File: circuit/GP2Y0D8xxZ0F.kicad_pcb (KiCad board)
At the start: 2 copper layers, 26.7 x 24.1 mm, 13 parts, among them P1 CONN_01X04, U1 GP2Y0D81xZ0F

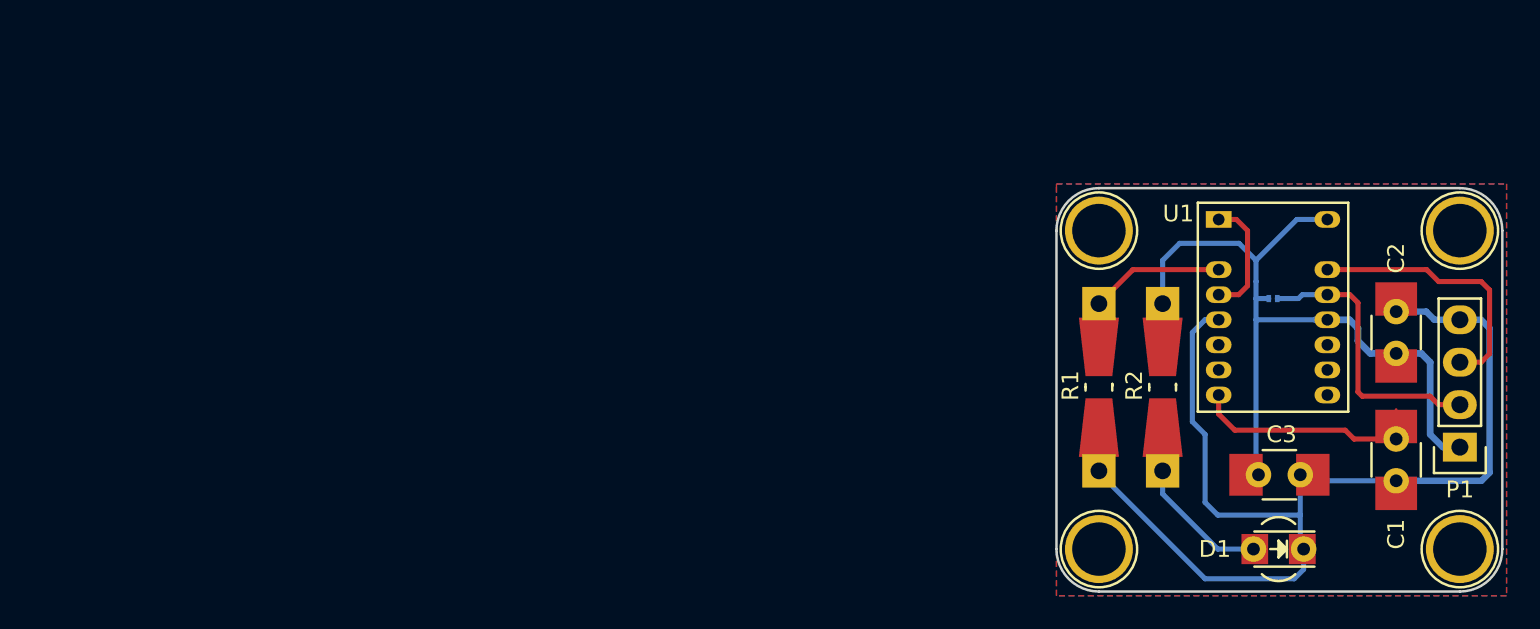
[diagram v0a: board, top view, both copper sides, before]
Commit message: First convert try and resize
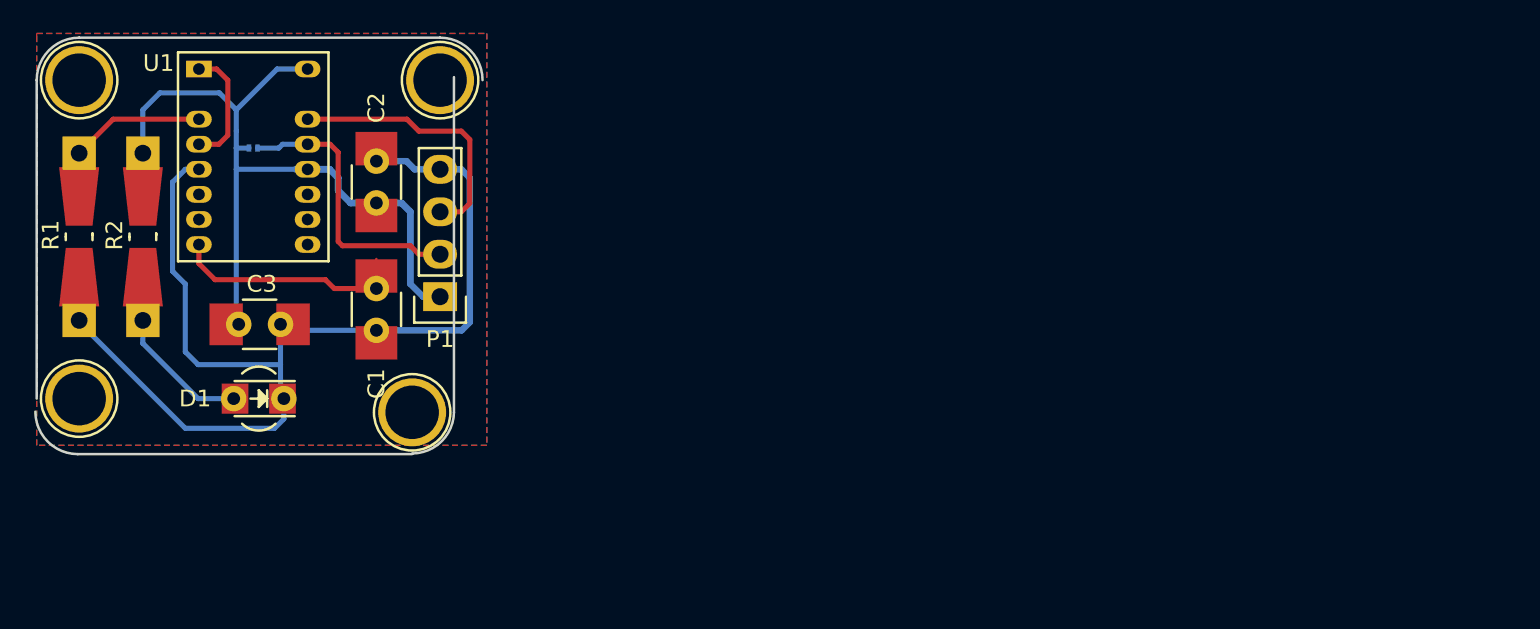
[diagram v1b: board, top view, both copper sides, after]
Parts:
- moved REF** 63.2 mm to (91.0, 98.5)
- moved C1 61.7 mm to (88.9, 92.3)
- moved C2 61.7 mm to (88.9, 84.7)
- moved R1 61.7 mm to (71.1, 88.0)
- moved REF** 61.7 mm to (71.1, 78.6)
- moved REF** 61.7 mm to (71.1, 97.7)
- moved C3 61.7 mm to (81.9, 93.2)
- moved JP1 61.7 mm to (81.5, 82.7)
- moved U1 61.7 mm to (81.5, 84.0)
- moved D1 61.7 mm to (81.8, 97.7)
- moved P1 61.7 mm to (92.7, 91.6)
- moved R2 61.7 mm to (74.9, 88.0)
- moved REF** 61.7 mm to (92.7, 78.6)
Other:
- board size 26.7 x 24.1 mm -> 26.8 x 24.9 mm

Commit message: changes in progress, open project with version 5 of kicad and the resizing started
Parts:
- moved REF** 1.68 mm to (91.0, 78.5)
- moved R2 1.02 mm to (74.0, 88.5)
- moved C3 0.91 mm to (81.0, 93.0)
- moved REF** 0.82 mm to (71.0, 98.5)
- moved R1 0.77 mm to (70.5, 88.5)
- moved U1 0.50 mm to (81.0, 84.0)
- moved REF** 0.15 mm to (71.0, 78.5)
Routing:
- net GND: track 70.0 -> 31.1 mm
- net VCC: track 50.8 -> 30.5 mm
- net Net-(D1-Pad2): track 10.8 -> 4.72 mm
- net /Output: track 16.0 -> 10.1 mm
- net /Enable: track 17.6 -> 13.2 mm
- net Net-(C1-Pad1): track 15.0 -> 13.9 mm
- removed copper zone on B.Cu, net GND
- removed copper zone on F.Cu, net GND
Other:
- board size 26.8 x 24.9 mm -> 25.1 x 25 mm

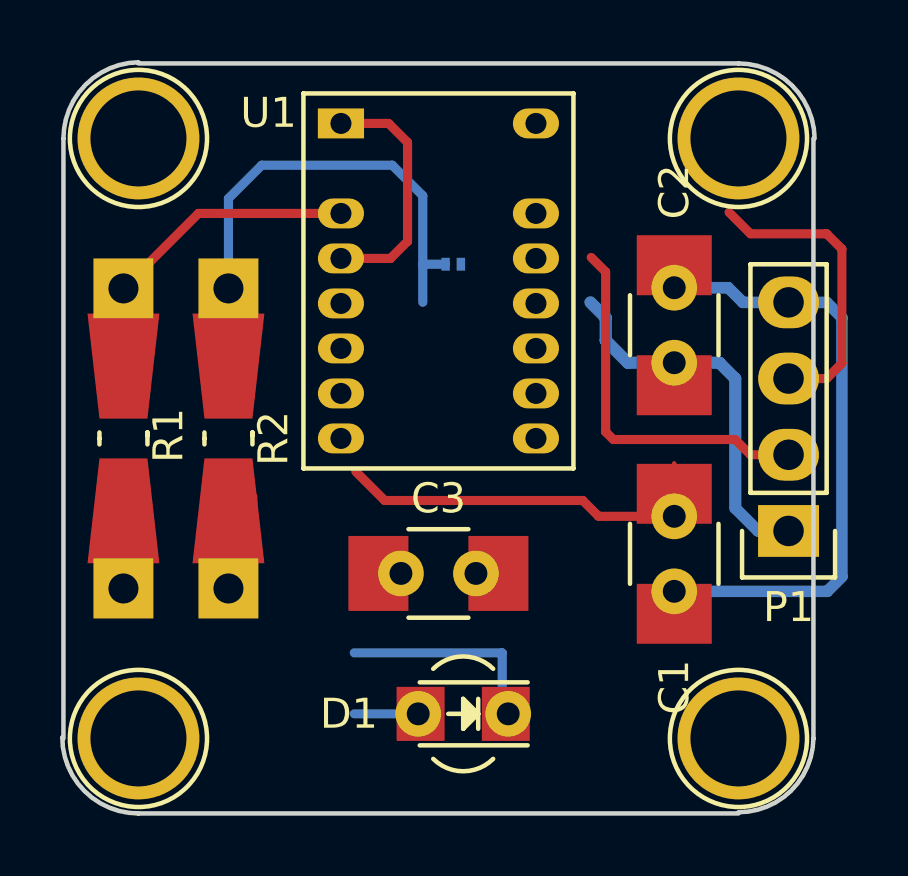
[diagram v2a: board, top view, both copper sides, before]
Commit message: New distribution of component in new size 25x25 mm
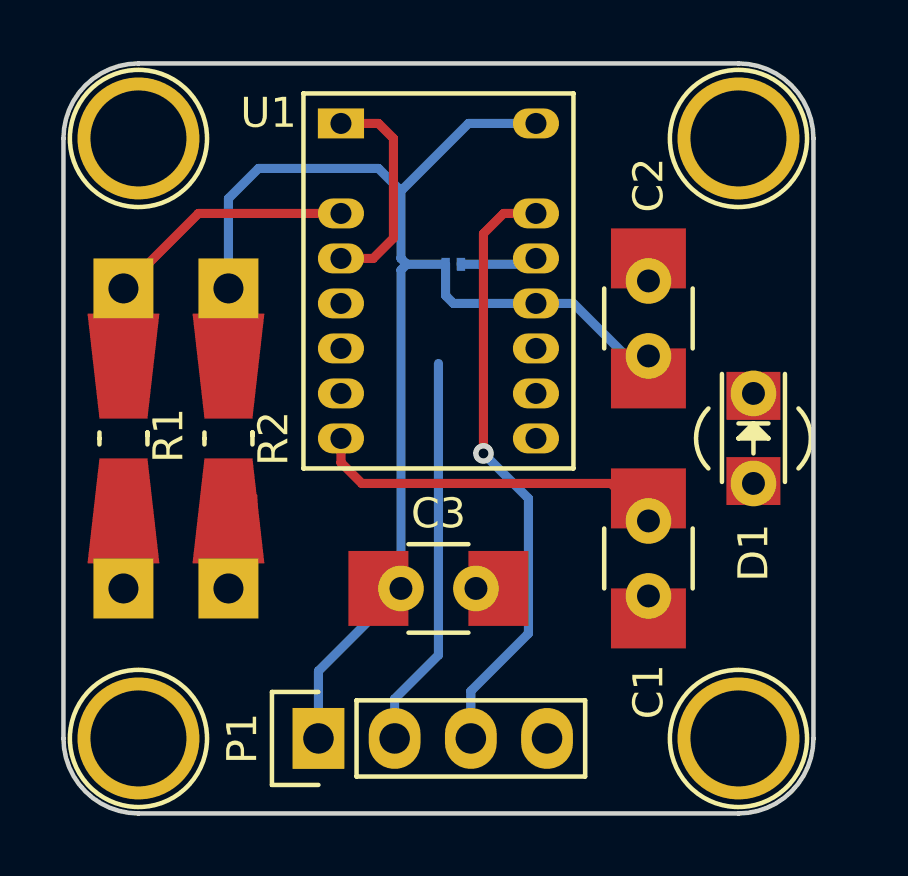
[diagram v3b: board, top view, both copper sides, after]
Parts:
- moved P1 17.1 mm to (77.0, 98.5), turned to 90 degrees
- moved D1 13.3 mm to (91.5, 88.5), turned to 270 degrees
- moved C2 0.89 mm to (88.0, 84.5)
- moved C1 0.87 mm to (88.0, 92.5)
- moved C3 0.50 mm to (81.0, 93.5)
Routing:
- net GND: track 31.1 -> 2.80 mm
- net VCC: track 30.5 -> 47.5 mm
- net /Output: track 10.1 -> 20.3 mm, vias 0 -> 1
- net /Enable: track 13.2 -> 15.7 mm
- net Net-(D1-Pad2): track 4.72 -> 2.59 mm
- net Net-(C1-Pad1): track 13.9 -> 11.9 mm
- net Net-(U1-Pad1): track 8.24 -> 7.31 mm
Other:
- board size 25.1 x 25 mm -> 25 x 25 mm

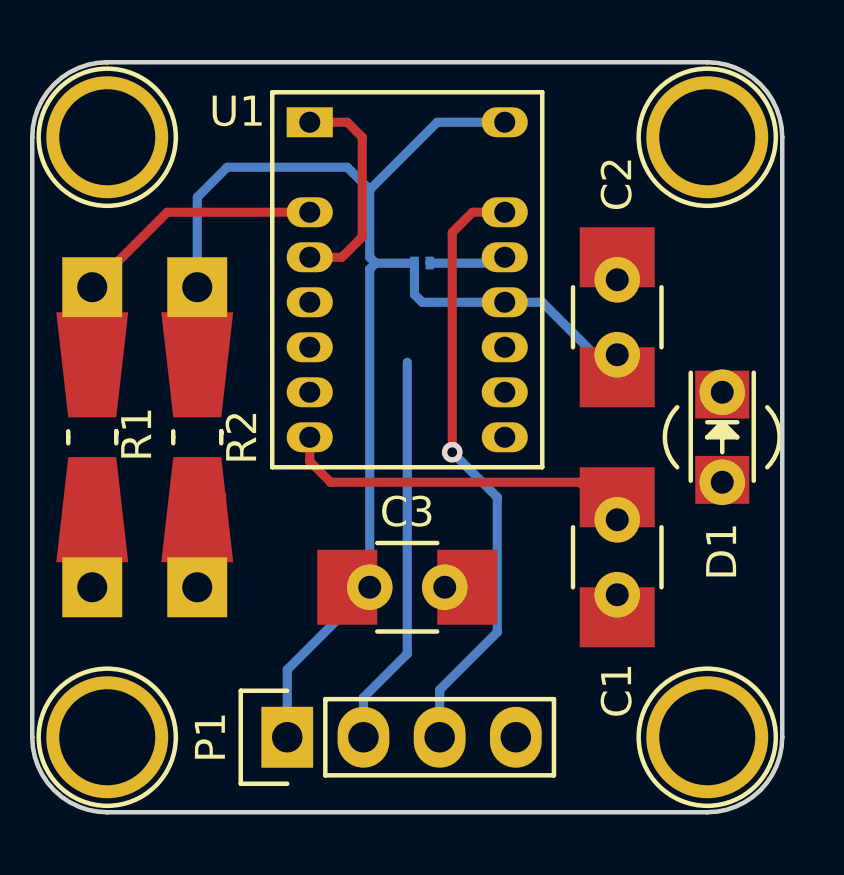
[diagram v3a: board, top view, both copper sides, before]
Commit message: Pcb resizing
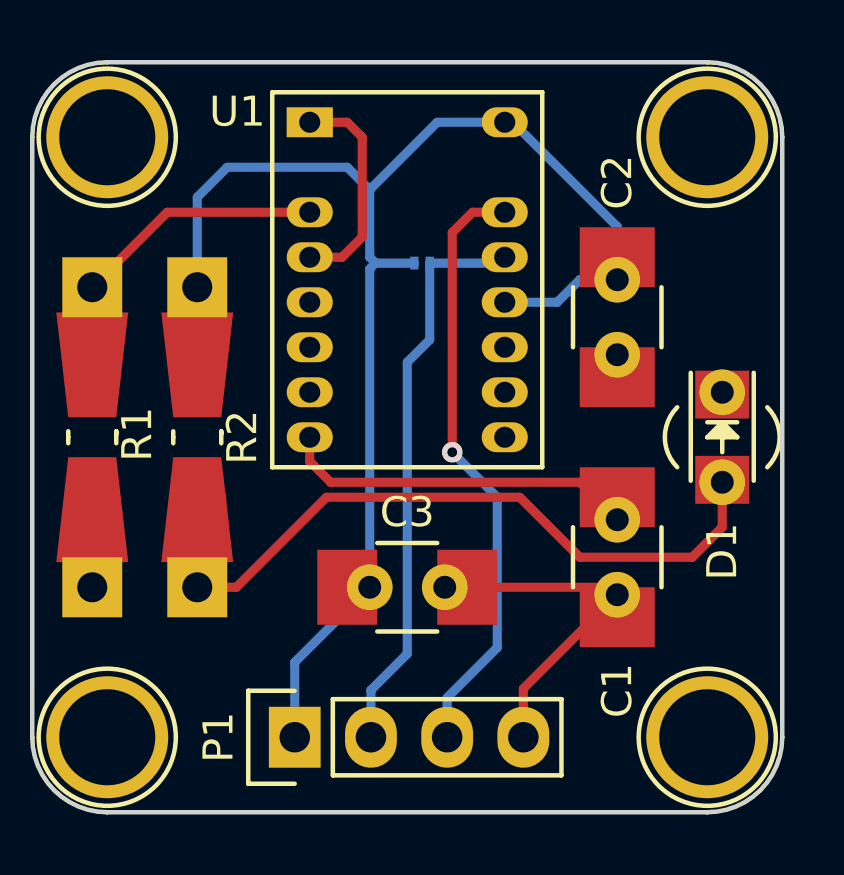
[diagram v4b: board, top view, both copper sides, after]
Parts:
- moved P1 0.25 mm to (77.2, 98.5)
- turned C2 to 270 degrees
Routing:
- net Net-(D1-Pad2): track 2.59 -> 24.2 mm
- net GND: track 2.80 -> 14.0 mm
- net /Enable: track 15.7 -> 19.2 mm
- net VCC: track 47.5 -> 49.8 mm
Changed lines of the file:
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@@
     (thickness 1.6002)
     (drawings 10)
-    (tracks 53)
+    (tracks 67)
     (zones 0)
     (modules 13)
@@
   )
   (module Pin_Headers:Pin_Header_Straight_1x04 (layer F.Cu)
-    (at 77 98.5 90)
+    (at 77.25 98.5 90)
     (descr "Through hole pin header")
     (tags "pin header")
@@
   )
   (module GP2Y0D81xZ0F:C_1210_HandSoldering_100n (layer F.Cu)
-    (at 88 84.5 90)
+    (at 88 84.5 270)
     (descr "Capacitor SMD 1210, hand soldering")
     (tags "capacitor 1210")
     (attr smd)
-    (fp_text reference C2 (at 4.445 0 90) (layer F.SilkS)
-      (effects (font (size 1 1) (thickness 0.15)))
-    )
-    (fp_text value 0.1uF (at 5.715 -1.27 90) (layer F.Fab) hide
+    (fp_text reference C2 (at -4.5 0 270) (layer F.SilkS)
+      (effects (font (size 1 1) (thickness 0.15)))
+    )
+    (fp_text value 0.1uF (at 5.715 -1.27 270) (layer F.Fab) hide
       (effects (font (size 1 1) (thickness 0.15)))
     )
@@
     (fp_line (start 1 -1.475) (end -1 -1.475) (layer F.SilkS) (width 0.15))
     (fp_line (start -1 1.475) (end 1 1.475) (layer F.SilkS) (width 0.15))
-    (pad 1 smd rect (at -2 0 90) (size 2 2.5) (layers F.Cu F.Paste F.Mask)
-      (net 3 VCC))
-    (pad 2 smd rect (at 2 0 90) (size 2 2.5) (layers F.Cu F.Paste F.Mask)
-      (net 2 GND))
-    (pad 1 thru_hole circle (at -1.25 0 90) (size 1.524 1.524) (drill 0.762) (layers *.Cu *.Mask F.SilkS)
-      (net 3 VCC))
-    (pad 2 thru_hole circle (at 1.25 0 90) (size 1.524 1.524) (drill 0.762) (layers *.Cu *.Mask F.SilkS)
+    (pad 1 smd rect (at -2 0 270) (size 2 2.5) (layers F.Cu F.Paste F.Mask)
+      (net 3 VCC))
+    (pad 2 smd rect (at 2 0 270) (size 2 2.5) (layers F.Cu F.Paste F.Mask)
+      (net 2 GND))
+    (pad 1 thru_hole circle (at -1.25 0 270) (size 1.524 1.524) (drill 0.762) (layers *.Cu *.Mask F.SilkS)
+      (net 3 VCC))
+    (pad 2 thru_hole circle (at 1.25 0 270) (size 1.524 1.524) (drill 0.762) (layers *.Cu *.Mask F.SilkS)
       (net 2 GND))
     (model Capacitors_SMD.3dshapes/C_1210_HandSoldering.wrl
@@
   (segment (start 71.08 93.00126) (end 71.08 90.413) (width 0.1524) (layer F.Cu) (net 2))
   (segment (start 71.08 93.00126) (end 71.08 93.108) (width 0.1524) (layer B.Cu) (net 2))
+  (segment (start 87.75 93.5) (end 88 93.75) (width 0.3048) (layer F.Cu) (net 2))
+  (segment (start 83 93.5) (end 87.75 93.5) (width 0.3048) (layer F.Cu) (net 2))
+  (segment (start 87.238001 94.511999) (end 88 93.75) (width 0.3048) (layer F.Cu) (net 2))
+  (segment (start 84.87 96.88) (end 87.238001 94.511999) (width 0.3048) (layer F.Cu) (net 2))
+  (segment (start 84.87 98.5) (end 84.87 96.88) (width 0.3048) (layer F.Cu) (net 2))
   (segment (start 74.89 82.99874) (end 74.89 85.587) (width 0.1524) (layer F.Cu) (net 3))
   (segment (start 84.744 77.964) (end 84.192 77.964) (width 0.4064) (layer B.Cu) (net 3))
@@
   (segment (start 81.239 82.694) (end 79.944 82.694) (width 0.3048) (layer B.Cu) (net 3))
   (segment (start 79.75 82.5) (end 79.75 80.25) (width 0.3048) (layer B.Cu) (net 3))
-  (segment (start 81.239 82.694) (end 81.239 83.739) (width 0.3048) (layer B.Cu) (net 3))
-  (segment (start 81.5 84) (end 84.25 84) (width 0.3048) (layer B.Cu) (net 3))
-  (segment (start 81.239 83.739) (end 81.5 84) (width 0.3048) (layer B.Cu) (net 3))
-  (segment (start 77 96.25) (end 79.75 93.5) (width 0.3048) (layer B.Cu) (net 3))
-  (segment (start 77 98.5) (end 77 96.25) (width 0.3048) (layer B.Cu) (net 3))
   (segment (start 79.75 82.888) (end 79.944 82.694) (width 0.3048) (layer B.Cu) (net 3))
   (segment (start 79.75 93.5) (end 79.75 82.888) (width 0.3048) (layer B.Cu) (net 3))
-  (segment (start 87.25 85.75) (end 88 85.75) (width 0.3048) (layer B.Cu) (net 3))
-  (segment (start 84.25 84) (end 85.5 84) (width 0.3048) (layer B.Cu) (net 3))
-  (segment (start 85.5 84) (end 87.25 85.75) (width 0.3048) (layer B.Cu) (net 3))
+  (segment (start 84.25 84) (end 86 84) (width 0.3048) (layer B.Cu) (net 3))
+  (segment (start 86.75 83.25) (end 88 83.25) (width 0.3048) (layer B.Cu) (net 3))
+  (segment (start 86 84) (end 86.75 83.25) (width 0.3048) (layer B.Cu) (net 3))
+  (segment (start 84.52 78) (end 84.25 78) (width 0.3048) (layer B.Cu) (net 3))
+  (segment (start 88 81.48) (end 84.52 78) (width 0.3048) (layer B.Cu) (net 3))
+  (segment (start 88 83.25) (end 88 81.48) (width 0.3048) (layer B.Cu) (net 3))
+  (segment (start 77.25 96) (end 79.75 93.5) (width 0.3048) (layer B.Cu) (net 3))
+  (segment (start 77.25 98.5) (end 77.25 96) (width 0.3048) (layer B.Cu) (net 3))
   (segment (start 74.89 93.00126) (end 74.89 90.413) (width 0.1524) (layer F.Cu) (net 4))
+  (segment (start 75.30429 93.50126) (end 74 93.50126) (width 0.3048) (layer F.Cu) (net 4))
+  (segment (start 91.5 91.5) (end 90.5 92.5) (width 0.3048) (layer F.Cu) (net 4))
+  (segment (start 90.5 92.5) (end 86.75 92.5) (width 0.3048) (layer F.Cu) (net 4))
+  (segment (start 86.75 92.5) (end 84.75 90.5) (width 0.3048) (layer F.Cu) (net 4))
+  (segment (start 84.75 90.5) (end 78.30555 90.5) (width 0.3048) (layer F.Cu) (net 4))
+  (segment (start 91.5 89.91986) (end 91.5 91.5) (width 0.3048) (layer F.Cu) (net 4))
+  (segment (start 78.30555 90.5) (end 75.30429 93.50126) (width 0.3048) (layer F.Cu) (net 4))
   (segment (start 84.056 82.694) (end 84.25 82.5) (width 0.3048) (layer B.Cu) (net 5))
   (segment (start 81.749 82.694) (end 84.056 82.694) (width 0.3048) (layer B.Cu) (net 5))
-  (segment (start 79.54 97.1792) (end 81 95.7192) (width 0.3048) (layer B.Cu) (net 5))
-  (segment (start 79.54 98.5) (end 79.54 97.1792) (width 0.3048) (layer B.Cu) (net 5))
   (segment (start 81 95.7192) (end 81 86) (width 0.3048) (layer B.Cu) (net 5))
+  (segment (start 81.749 85.251) (end 81 86) (width 0.3048) (layer B.Cu) (net 5))
+  (segment (start 81.749 82.694) (end 81.749 85.251) (width 0.3048) (layer B.Cu) (net 5))
+  (segment (start 79.79 96.9292) (end 79.79 98.5) (width 0.3048) (layer B.Cu) (net 5))
+  (segment (start 81 95.7192) (end 79.79 96.9292) (width 0.3048) (layer B.Cu) (net 5))
   (segment (start 83.1752 81) (end 82.5 81.6752) (width 0.3048) (layer F.Cu) (net 6))
   (segment (start 84.25 81) (end 83.1752 81) (width 0.3048) (layer F.Cu) (net 6))
@@
   (segment (start 82.5 89) (end 82.5 89) (width 0.3048) (layer F.Cu) (net 6))
   (via (at 82.5 89) (size 0.6858) (drill 0.3302) (layers F.Cu B.Cu) (net 6))
-  (segment (start 82.08 96.92) (end 82.08 98.5) (width 0.3048) (layer B.Cu) (net 6))
-  (segment (start 84 95) (end 82.08 96.92) (width 0.3048) (layer B.Cu) (net 6))
-  (segment (start 82.5 89) (end 84 90.5) (width 0.3048) (layer B.Cu) (net 6))
-  (segment (start 84 90.5) (end 84 95) (width 0.3048) (layer B.Cu) (net 6))
+  (segment (start 84 90.5) (end 82.5 89) (width 0.3048) (layer B.Cu) (net 6))
+  (segment (start 84 95.5092) (end 84 90.5) (width 0.3048) (layer B.Cu) (net 6))
+  (segment (start 82.33 97.1792) (end 84 95.5092) (width 0.3048) (layer B.Cu) (net 6))
+  (segment (start 82.33 98.5) (end 82.33 97.1792) (width 0.3048) (layer B.Cu) (net 6))
   (segment (start 71.08 82.99874) (end 71.28326 82.99874) (width 0.1524) (layer B.Cu) (net 7))
   (segment (start 70.5 83.49874) (end 70.50126 83.49874) (width 0.1524) (layer F.Cu) (net 7))
